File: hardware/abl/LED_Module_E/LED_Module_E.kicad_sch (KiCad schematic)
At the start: 92 parts, among them J1 SFW20S-2STE1LF, J3 009159008603906, Q1 Si3456DDV, Q11 Si3456DDV, Q12 Si3456DDV, Q2 Si3456DDV, Q3 Si3456DDV, Q4 Si3456DDV, Q5 Si3456DDV, Q6 Si3456DDV, Q7 Si3456DDV, Q8 Si3456DDV, U1 TMP1075DGK, U2 74HCT244, U3 24AA02UIDT-I/OT

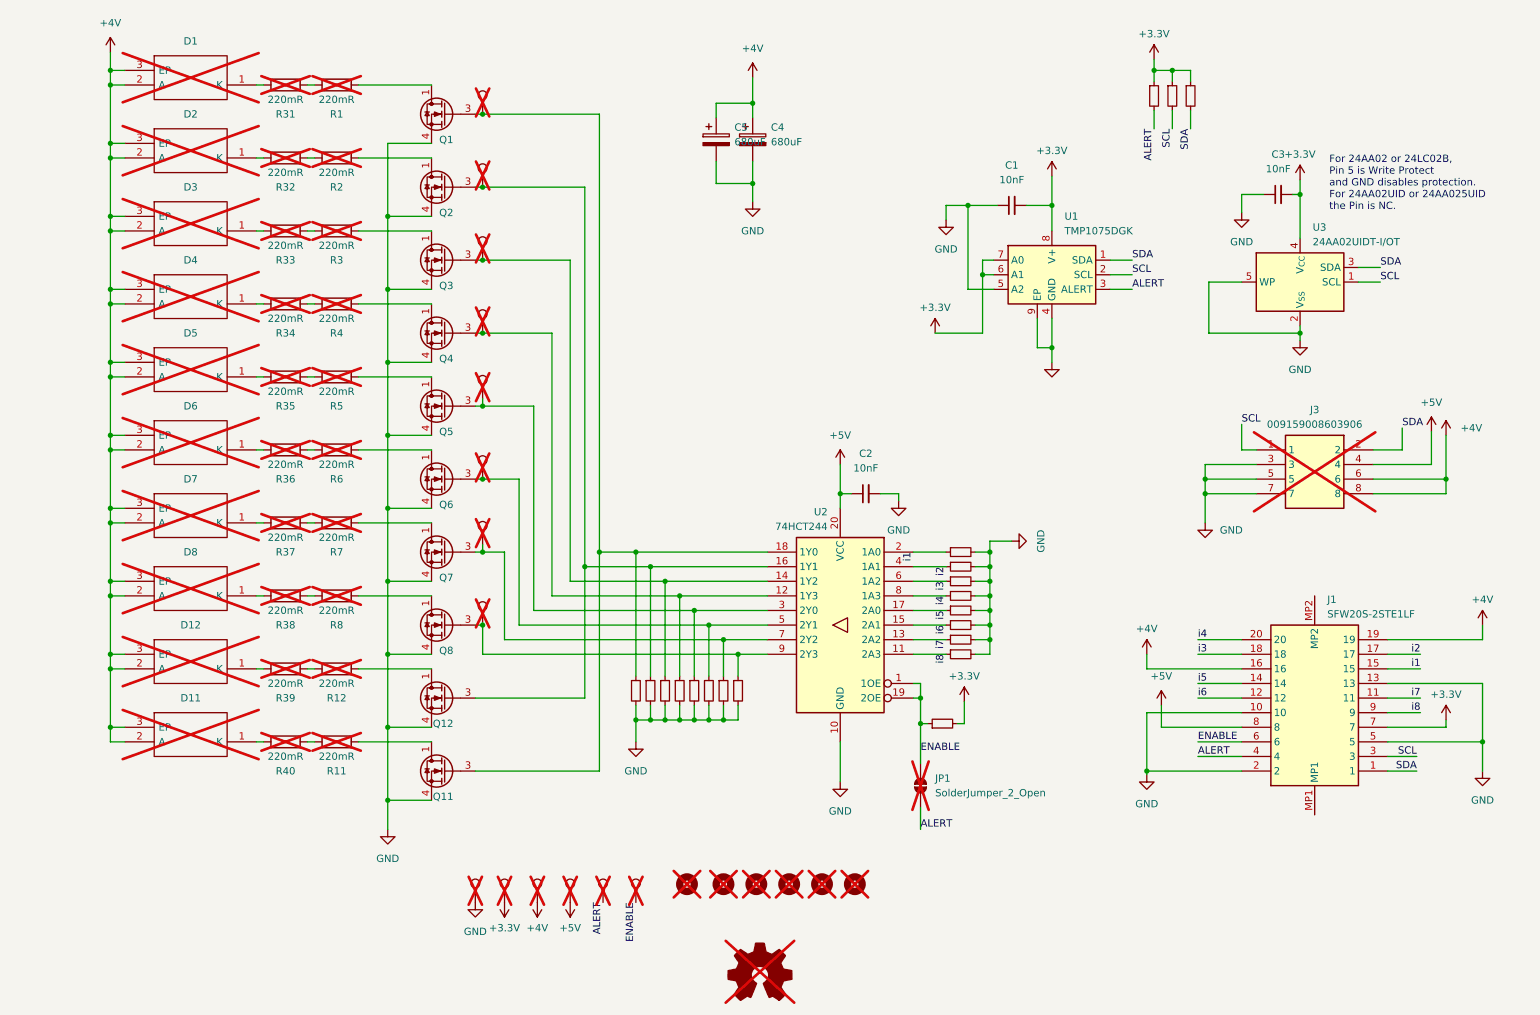
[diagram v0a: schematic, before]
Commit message: Move LED Module E to the ABL directory and update all affected READMEs.
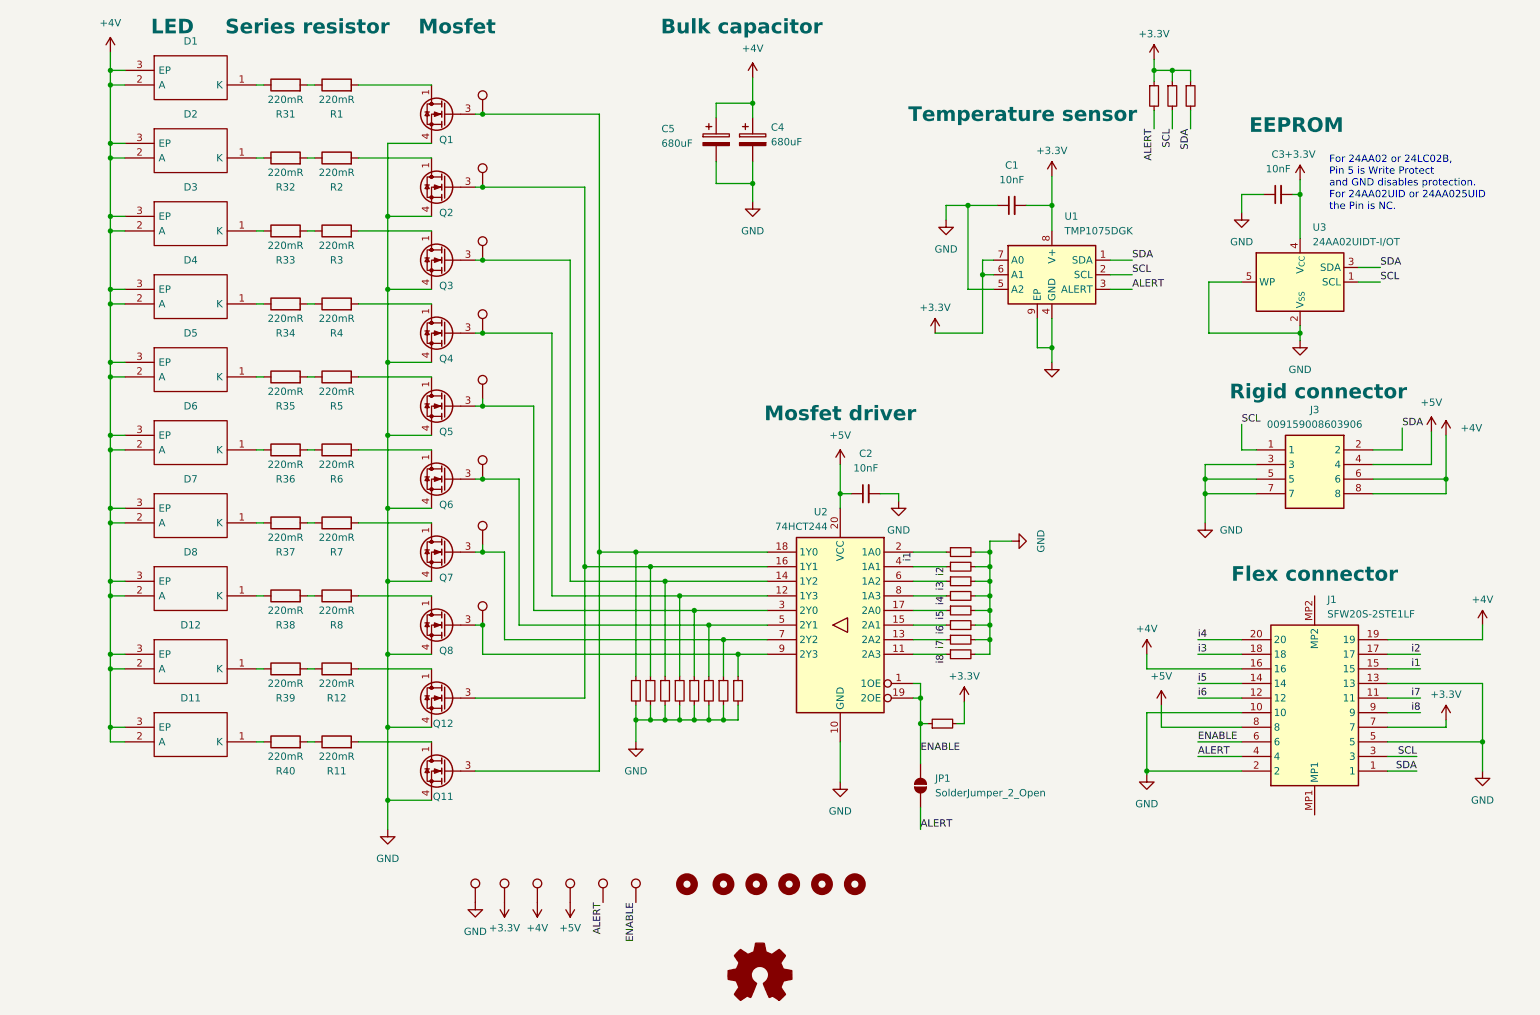
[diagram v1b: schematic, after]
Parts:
- C1: Ordered Now 0 -> (none); Ordered Previously 100 -> (none); Purpose (none) -> Decoupling capacitor
- C2, C3: Ordered Now 0 -> (none); Ordered Previously 20 -> (none); Purpose (none) -> Decoupling capacitor
- C4, C5: Ordered Now 10 -> (none); Ordered Previously 0 -> (none); Purpose (none) -> Bulk capacitor
- D1, D11, D12, D2, D3, D4, D5, D6, D7, D8: Height 1.13 -> (none); Ordered Now 38 -> (none); Ordered Previously 63 -> (none); Purpose (none) -> LED; now fitted
- H1, H2, H3, H4, H5, H6, LOGO1, TP1, TP10, TP11, TP12, TP13, TP14, TP2, TP3, TP4, TP5, TP6, TP7, TP8, TP9: Ordered Previously - -> (none); now fitted
- J1: Height 5.5 -> (none); Purpose (none) -> Flex connector
- J3: Height 5.25 -> (none); Mouser Part Number 581-009159008603906 -> (none); Mouser Price/Stock https://www.mouser.co.uk/ProductDetail/KYOCERA-AVX/00915900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 -> (none); Purpose (none) -> Rigid connector; now fitted
- JP1: Ordered Previously - -> (none); Purpose (none) -> Direct alert; now fitted
- Q1, Q11, Q12, Q2, Q3, Q4, Q5, Q6, Q7, Q8: Ordered Now 0 -> (none); Ordered Previously 100 -> (none); Purpose (none) -> Mosfet
- R1, R11, R12, R2, R3, R31, R32, R33, R34, R35, R36, R37, R38, R39, R4, R40, R5, R6, R7, R8: Ordered Now 50 -> (none); Ordered Previously 95 -> (none); Purpose (none) -> Series resistor; now fitted
- R10, R13, R14, R15, R16, R17, R18, R19, R20, R21, R22, R23, R24, R25, R26, R27, R28, R29, R30, R9: Ordered Now 100 -> (none); Ordered Previously 0 -> (none); Purpose (none) -> Pullup
- U1: Ordered Now 20 -> (none); Ordered Previously 10 -> (none); Purpose (none) -> Temperature sensor
- U2: Ordered Previously 20 -> (none); Purpose (none) -> Mosfet driver
- U3: Ordered Previously 20 -> (none); Purpose (none) -> EEPROM

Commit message: Implemented a lot of recommended changes, including layer swap.
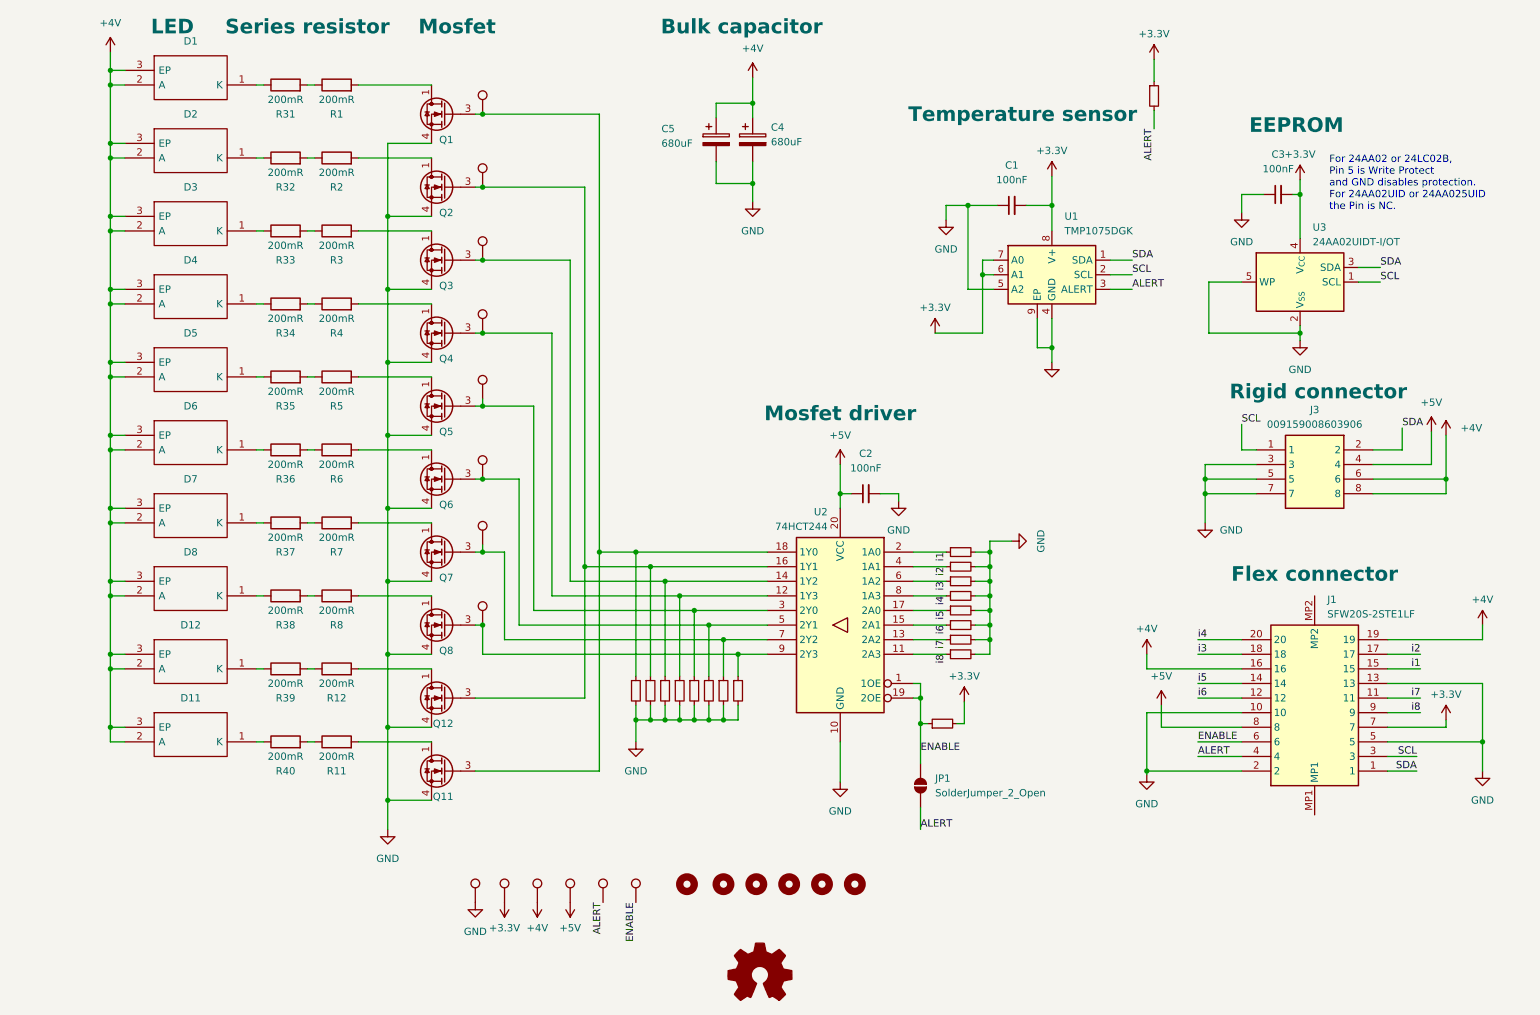
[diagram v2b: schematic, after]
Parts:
- removed R29, R30: 2740R, Resistor_SMD:R_0603_1608Metric, symbol Device:R_Small
- C1: value 10nF -> 100nF; LCSC Part # C15195 -> (none); Manufacturer_Part_Number CL05B103KB5NNNC -> (none)
- C2, C3: value 10nF -> 100nF; LCSC Part # C57112 -> (none); Manufacturer_Part_Number 0603B103K500NT -> (none)
- R1, R11, R12, R2, R3, R31, R32, R33, R34, R35, R36, R37, R38, R39, R4, R40, R5, R6, R7, R8: value 220mR -> 200mR; LCSC Part # (none) -> C4000899; Manufacturer_Part_Number (none) -> RCWE1020R200FKEA; Note (none) -> I calculated 220mR but 200mR is much cheaper
- R10, R13, R14, R15, R16, R17, R18, R20, R21, R22, R23, R24, R25, R26, R27, R9: value 2740R -> 4700R; LCSC Part # C13167 -> (none); Manufacturer_Part_Number 0603WAF2701T5E -> (none)

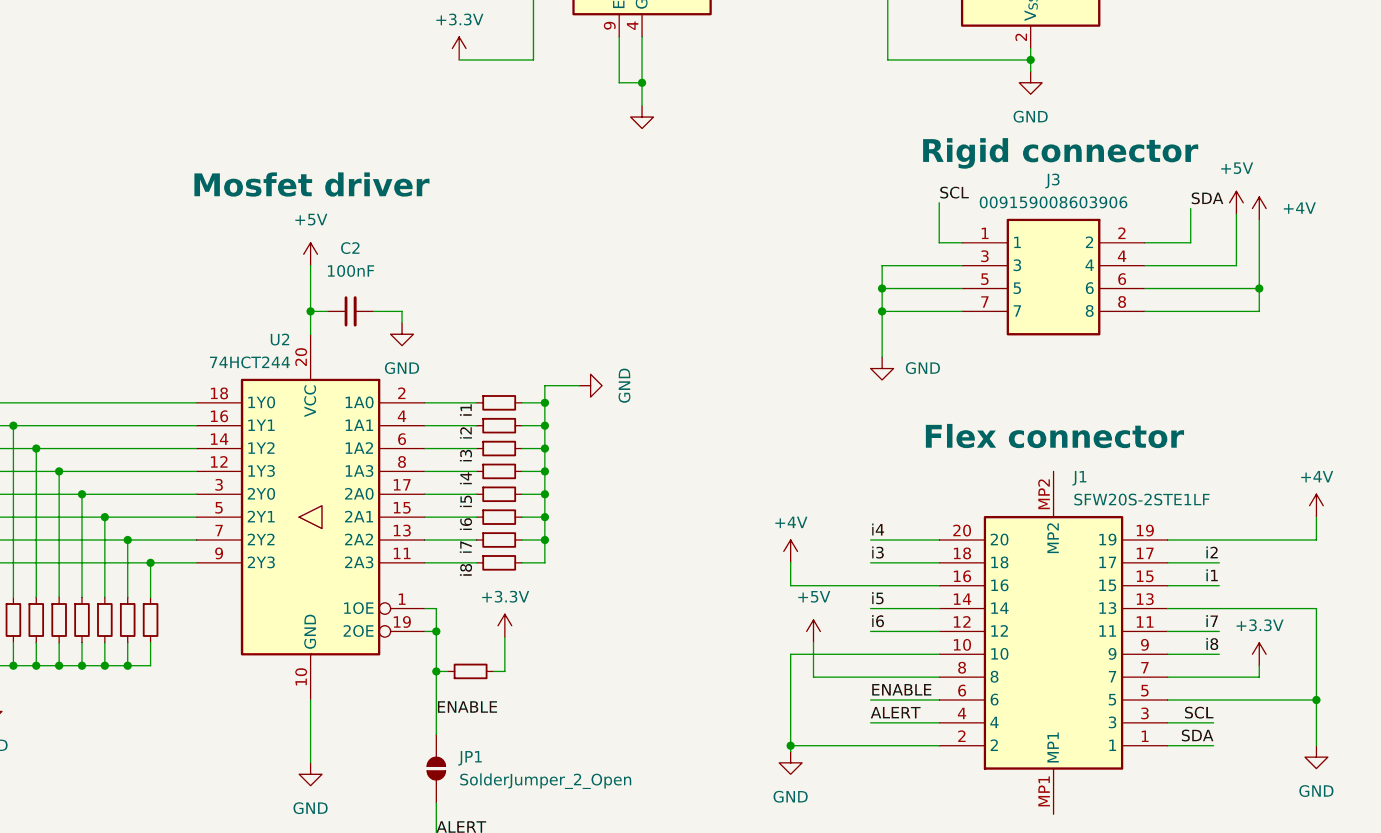
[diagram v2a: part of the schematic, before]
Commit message: Changed driver, mirrored LEDs and general cleanup.
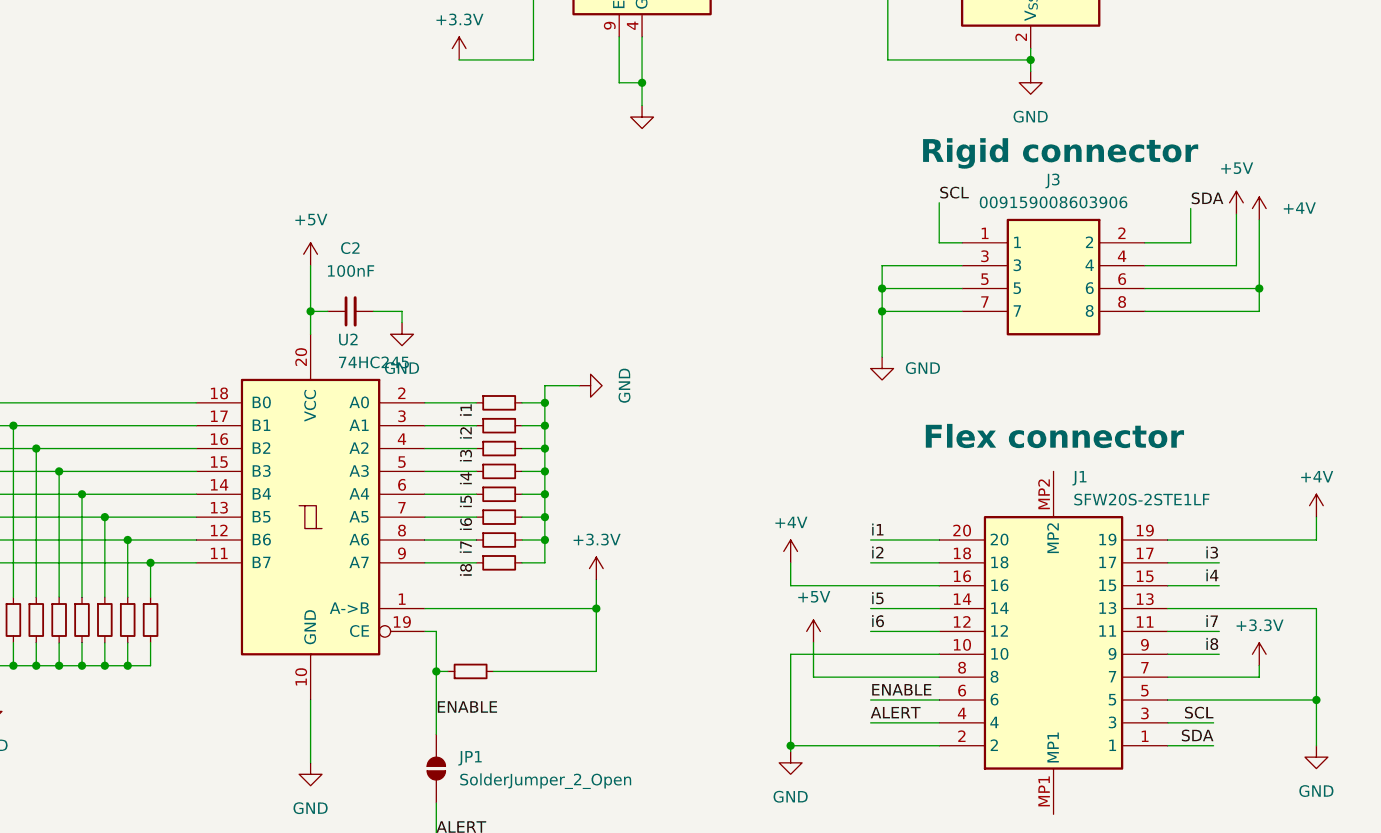
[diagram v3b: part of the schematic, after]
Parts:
- removed U2: 74HCT244, Package_SO:SOIC-20W_7.5x12.8mm_P1.27mm, symbol 74xx:74HCT244
- added U2: 74HC245, Package_SO:TSSOP-20_4.4x6.5mm_P0.65mm, symbol 74xx:74HC245
- R10, R13, R14, R15, R16, R17, R18, R20, R21, R22, R23, R24, R25, R26, R27, R9: footprint Resistor_SMD:R_0603_1608Metric -> Resistor_SMD:R_0402_1005Metric
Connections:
- net +3.3V: now also U2.1 (A->B)
- net +5V: now also U2.20 (VCC)
- net ENABLE: now also U2.19 (CE)
- net GND: now also U2.10 (GND)
- net i1: now also J1.20, U2.2 (A0); no longer J1.15
- net i2: now also J1.18, U2.3 (A1); no longer J1.17
- net i3: now also J1.17, U2.4 (A2); no longer J1.18
- net i4: now also J1.15, U2.5 (A3); no longer J1.20
- net i5: now also U2.6 (A4)
- net i6: now also U2.7 (A5)
- net i7: now also U2.8 (A6)
- net i8: now also U2.9 (A7)
- net at Q12.3 (G), Q2.3 (G), R21.1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: now also U2.17 (B1)
- net at Q3.3 (G), R22.1, TP9.1: now also U2.16 (B2)
- net at Q4.3 (G), R23.1, TP10.1: now also U2.15 (B3)
- net at Q1.3 (G), Q11.3 (G), R20.1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: now also U2.18 (B0)
- net at Q8.3 (G), R27.1, TP14.1: now also U2.11 (B7)
- net at Q7.3 (G), R26.1, TP13.1: now also U2.12 (B6)
- net at Q5.3 (G), R24.1, TP11.1: now also U2.14 (B4)
- net at Q6.3 (G), R25.1, TP12.1: now also U2.13 (B5)
